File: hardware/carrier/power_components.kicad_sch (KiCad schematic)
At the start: 38 parts, among them J13 USB4235, J14 BATTERY, Q2 AO3401A, SW4 JS102011SAQN, U16 MAX17048G+T10, U2 BQ25185DLHR, U4 TPS62840DLCR

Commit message: AI resized many of the components
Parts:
- C10: footprint Capacitor_SMD:C_0603_1608Metric -> Capacitor_SMD:C_0402_1005Metric; LCSC C21122 -> C337699; MPN CL10B223KB8NNNC -> CL05B223KB5NNNC
- C18, C19, C47: footprint Capacitor_SMD:C_0603_1608Metric -> Capacitor_SMD:C_0402_1005Metric; LCSC C19702 -> C15525; MPN CL10A106KP8NNNC -> CL05A106MQ5NUNC
- C2, C46: footprint Capacitor_SMD:C_0603_1608Metric -> Capacitor_SMD:C_0402_1005Metric; LCSC C14663 -> C1525; MPN CL10B104KB8NNNC -> CL05B104KO5NNNC
- D5: value USBLC6-2SC6 -> USBLC6-2P6; footprint Package_TO_SOT_SMD:SOT-23-6 -> Package_TO_SOT_SMD:SOT-666; LCSC C7519 -> C2827693; MPN USBLC6-2SC6 -> USBLC6-2P6
- R10, R23, R25, R26: footprint Resistor_SMD:R_0603_1608Metric -> Resistor_SMD:R_0402_1005Metric; LCSC C25804 -> C25744; MPN 0603WAF1002T5E -> 0402WGF1002TCE
- R22: footprint Resistor_SMD:R_0603_1608Metric -> Resistor_SMD:R_0402_1005Metric; LCSC C25810 -> C25762; MPN 0603WAF1802T5E -> 0402WGF1802TCE
- R24: footprint Resistor_SMD:R_0603_1608Metric -> Resistor_SMD:R_0402_1005Metric; LCSC C32183 -> C8369; MPN 0603WAF6040T5E -> 0402WGF6040TCE
- R27, R7: footprint Resistor_SMD:R_0603_1608Metric -> Resistor_SMD:R_0402_1005Metric; LCSC C23186 -> C25905; MPN 0603WAF5101T5E -> 0402WGF5101TCE
- R28: footprint Resistor_SMD:R_0603_1608Metric -> Resistor_SMD:R_0402_1005Metric; LCSC C22938 -> C11490; MPN 0603WAF2204T5E -> 0402WGF2204TCE
- R6, R73, R74: footprint Resistor_SMD:R_0603_1608Metric -> Resistor_SMD:R_0402_1005Metric; LCSC C21189 -> C17168; MPN 0603WAF0000T5E -> 0402WGF0000TCE
- R71: footprint Resistor_SMD:R_0603_1608Metric -> Resistor_SMD:R_0402_1005Metric; LCSC C23206 -> C25796; MPN 0603WAF5602T5E -> 0402WGF5602TCE
- R72, R75: footprint Resistor_SMD:R_0603_1608Metric -> Resistor_SMD:R_0402_1005Metric; LCSC C25803 -> C25741; MPN 0603WAF1003T5E -> 0402WGF1003TCE
- R76: footprint Resistor_SMD:R_0603_1608Metric -> Resistor_SMD:R_0402_1005Metric; LCSC C188011 -> C270622; MPN RM06FTN2673 -> 0402WGF2673TCE

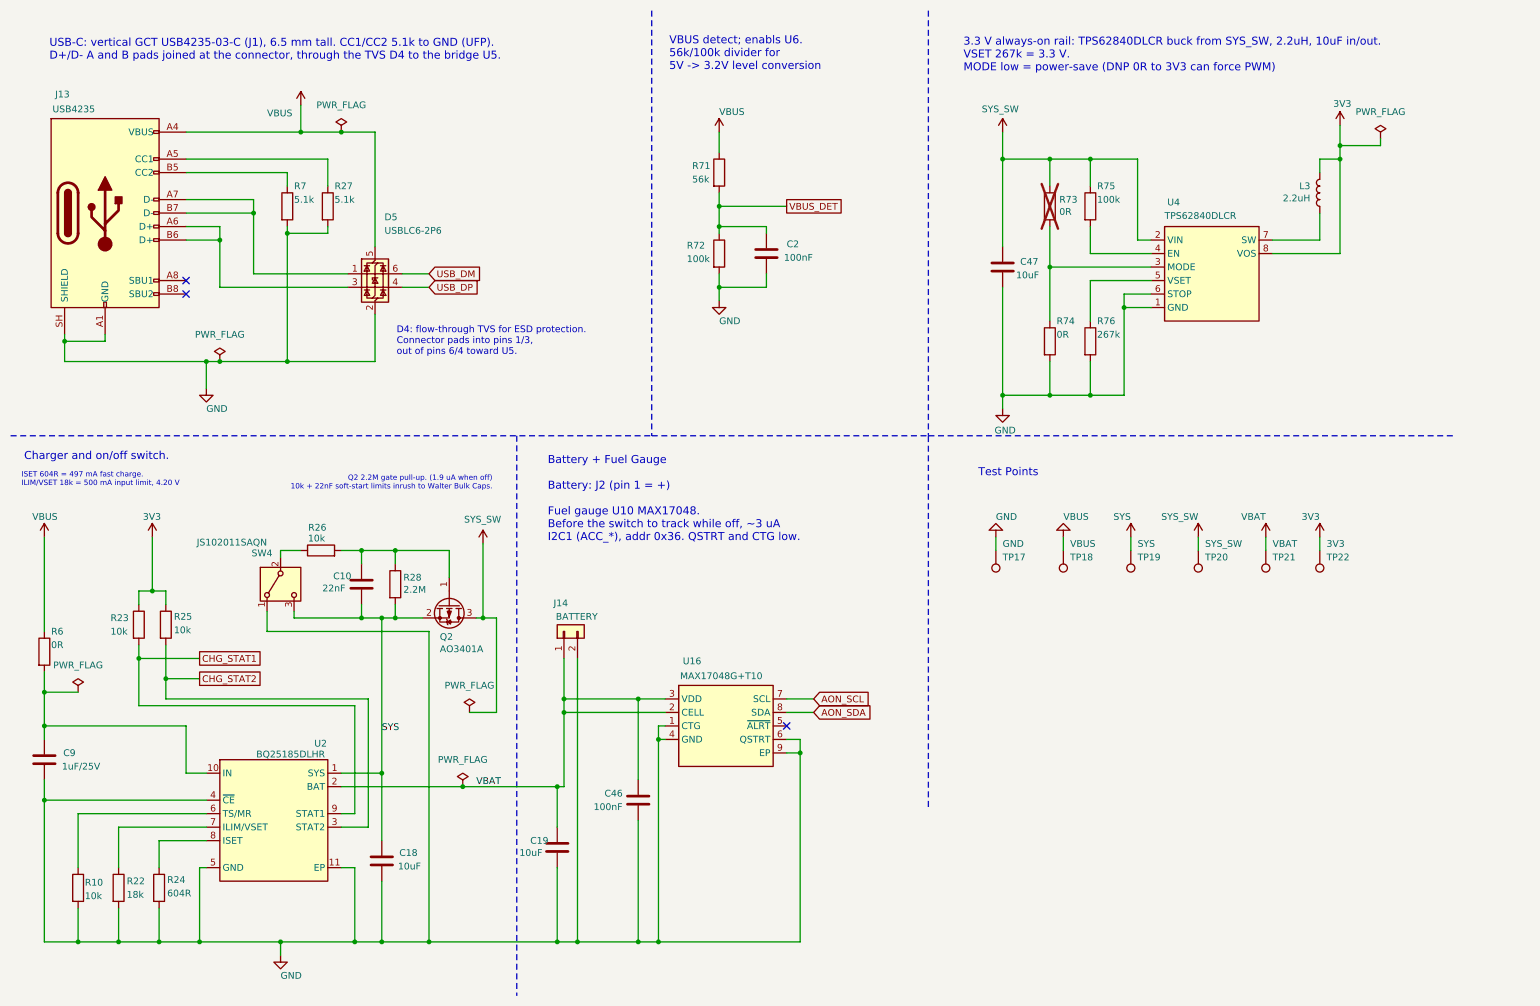
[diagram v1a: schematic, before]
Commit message: components renumbered
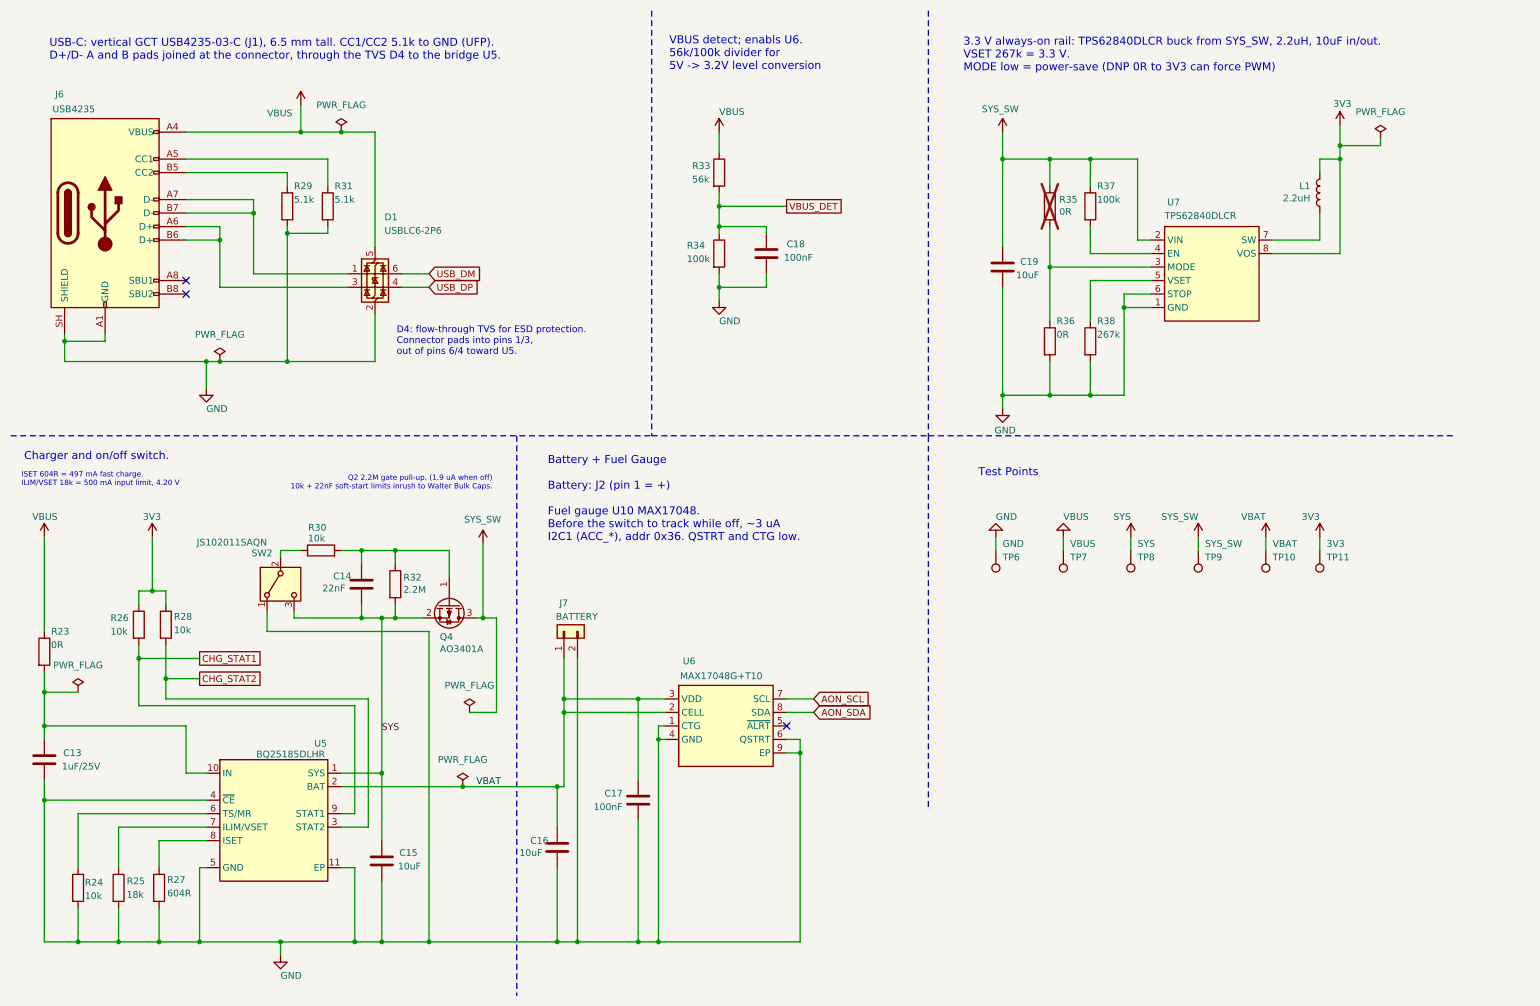
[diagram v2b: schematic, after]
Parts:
- renumbered C9 to C13, C10 to C14, C18 to C15, C19 to C16, C46 to C17, C2 to C18, C47 to C19, D5 to D1, J13 to J6, J14 to J7, L3 to L1, Q2 to Q4, R6 to R23, R10 to R24, R22 to R25, R23 to R26, R24 to R27, R25 to R28, R7 to R29, R26 to R30, R27 to R31, R28 to R32, R71 to R33, R72 to R34, R73 to R35, R74 to R36, R75 to R37, R76 to R38, SW4 to SW2, TP21 to TP10, TP22 to TP11, TP17 to TP6, TP18 to TP7, TP19 to TP8, TP20 to TP9, U2 to U5, U16 to U6, U4 to U7

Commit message: Attempt to layout the PCB
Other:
- moved on the sheet: C16, C17, U6
